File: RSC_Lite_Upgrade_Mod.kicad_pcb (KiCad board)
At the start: 2 copper layers, 21.8 x 42.4 mm, 22 parts, among them J3 SWD, J4 JTAG, U1 32F103C8T6, Y1 8Mhz

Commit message: Reorganize REV.2 board
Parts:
- moved J4 16.0 mm to (200.4, 86.6), turned to -90 degrees
- moved C10 3.18 mm to (184.7, 85.3)
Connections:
- J4 pad 1: VCC -> /JTAG_TMS
- J4 pad 2: GND -> /JTAG_TDI
- J4 pad 3: /JTAG_TDO -> /JTAG_TCK
- J4 pad 4: /JTAG_TCK -> /JTAG_TDO
- J4 pad 5: /JTAG_TDI -> GND
- J4 pad 6: /JTAG_TMS -> VCC
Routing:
- net /JTAG_TMS: track 5.78 -> 23.4 mm, vias 0 -> 1
- net /JTAG_TDI: track 7.91 -> 22.3 mm
- net /JTAG_TCK: track 9.87 -> 19.3 mm
- net GND: track 245.4 -> 251.8 mm, vias 29 -> 28
- net /JTAG_TDO: track 15.6 -> 21.1 mm
- net VCC: track 174.7 -> 173.5 mm, vias 6 -> 8

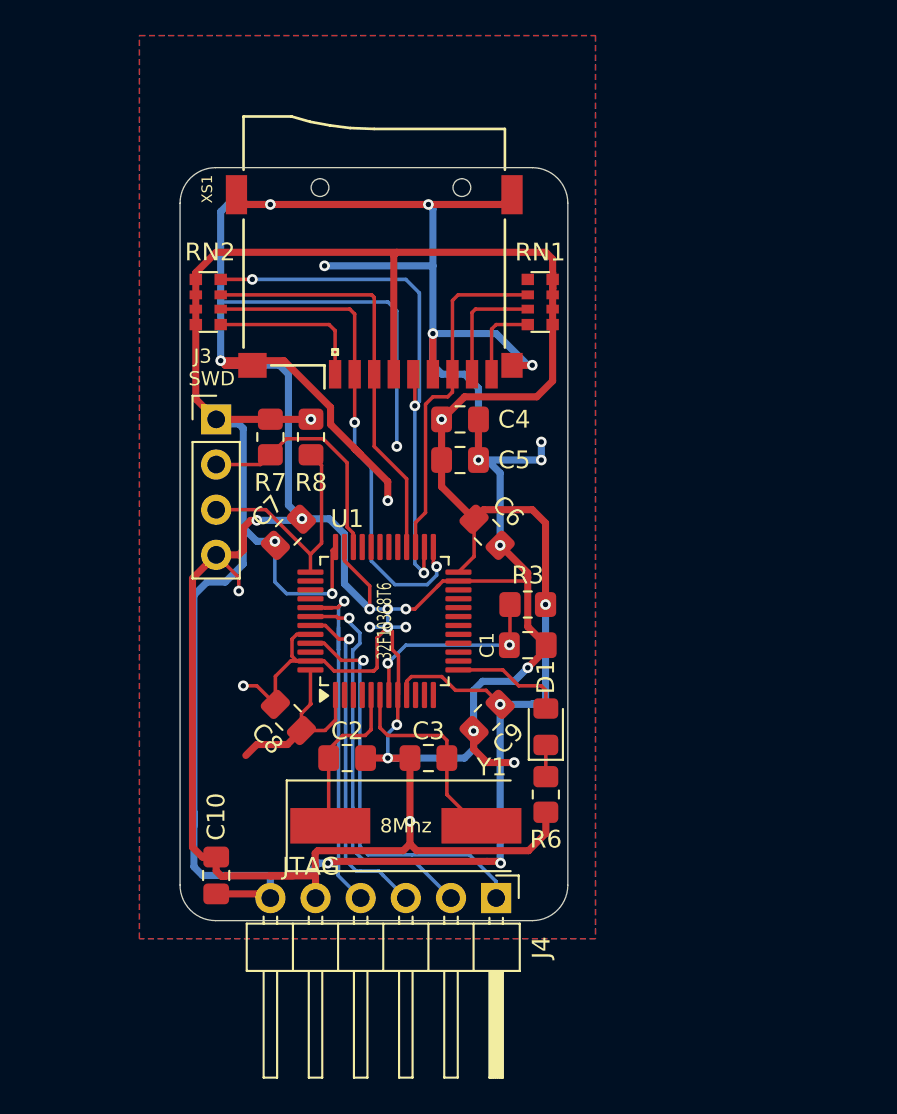
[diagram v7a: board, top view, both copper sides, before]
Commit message: Reroute the board, move the jtag connector
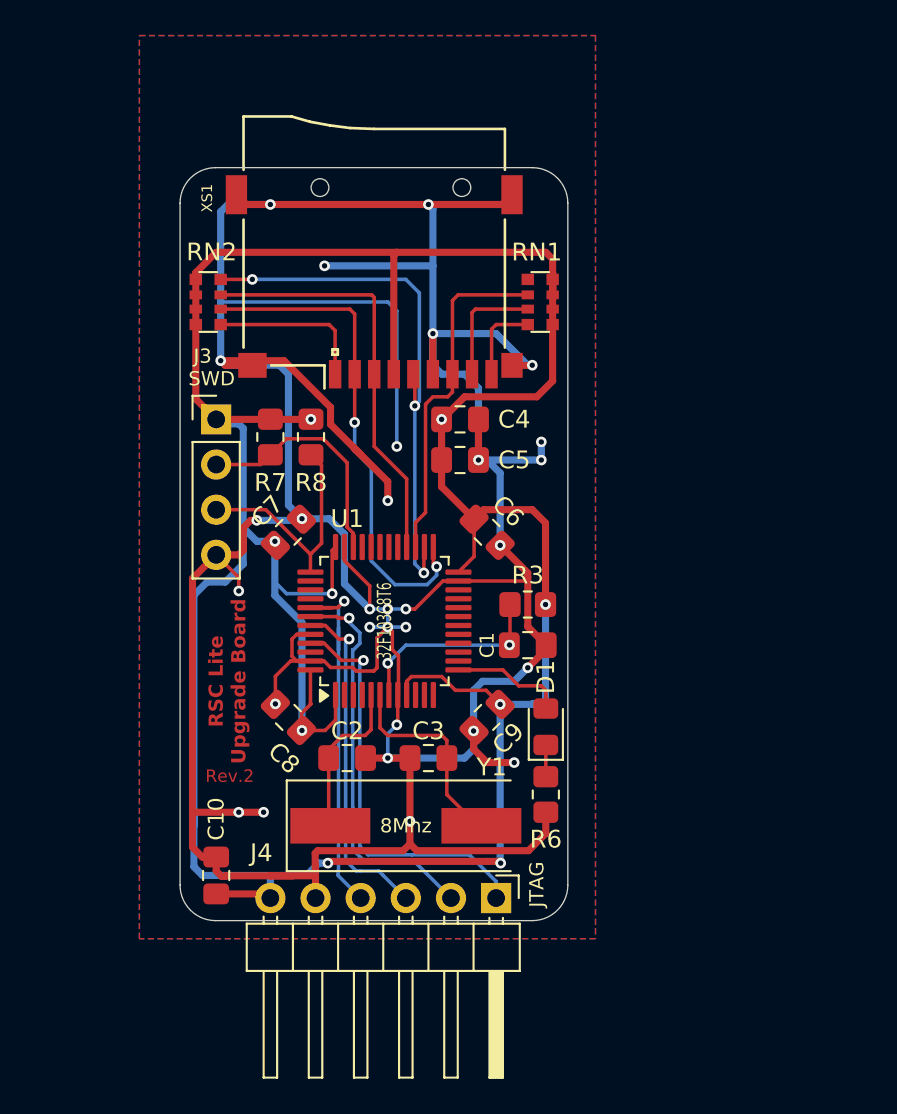
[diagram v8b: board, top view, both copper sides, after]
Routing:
- net VCC: track 173.5 -> 181.1 mm, vias 8 -> 9
- net GND: track 251.8 -> 253.7 mm, vias 28 -> 30
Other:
- board text added: "RSC Lite"
- board text added: "Upgrade Board"
- board text removed: "Lava RSC Lite Upgrade board"
